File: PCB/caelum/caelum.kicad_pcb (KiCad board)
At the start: 2 copper layers, 14 parts, among them J1 BATT+, J2 BATT-, J3 3V3, J4 OUT-, Q1 FS8205A, U1 DW01A, U2 MCP1700T-3302E

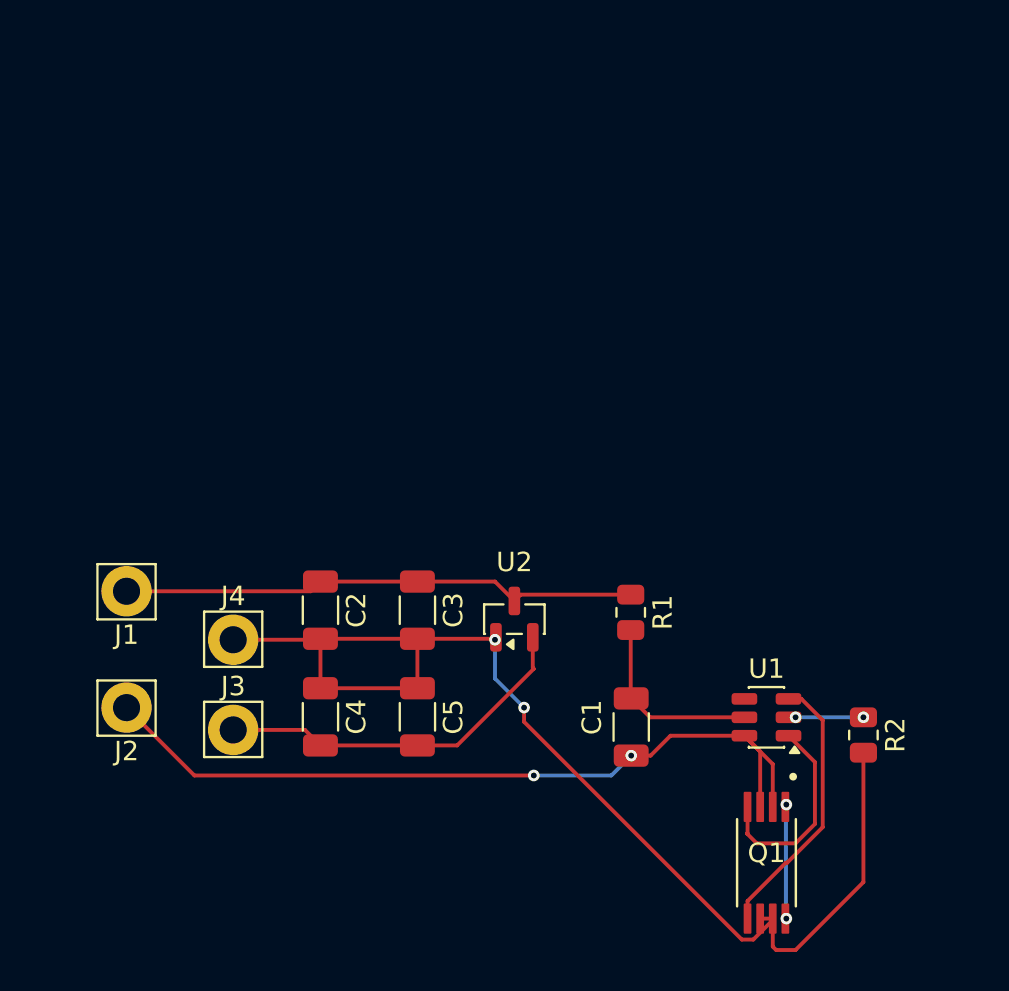
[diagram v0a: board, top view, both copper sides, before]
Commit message: Update partitions.csv for ESP32-H2 with 4MB Flash configuration
- Adjusted partition sizes and offsets to optimize for OTA updates.
- Reduced NVS size to 0x4000 and updated offsets for phy_init and otadata.
- Modified OTA partition sizes to fit within the new 4MB flash limit.
- Ensured compatibility with the new memory layout for better performance.
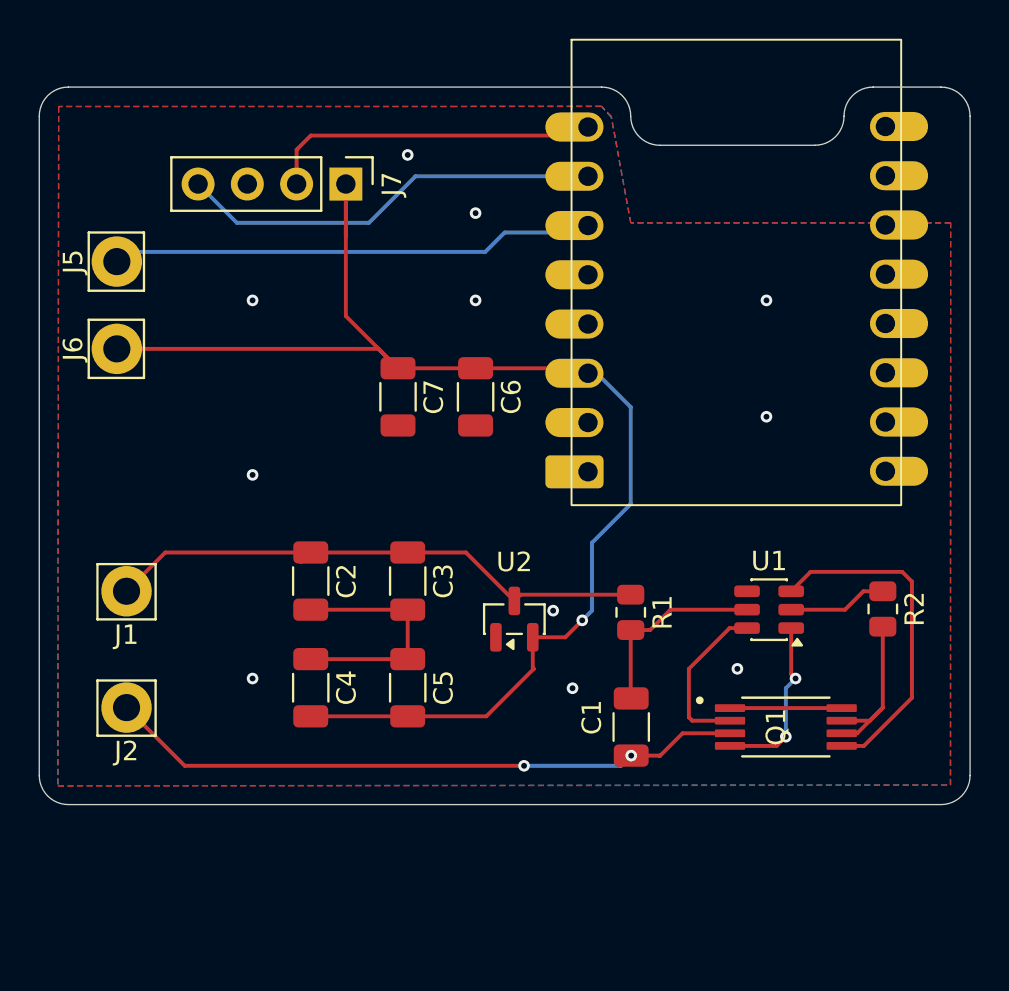
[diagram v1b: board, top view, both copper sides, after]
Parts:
- removed J3: 3V3, Connector_Pin:Pin_D1.4mm_L8.5mm_W2.8mm_FlatFork
- removed J4: OUT-, Connector_Pin:Pin_D1.4mm_L8.5mm_W2.8mm_FlatFork
- added C6: 1µF, Capacitor_SMD:C_1206_3216Metric, F.Cu at (80.0, 44.0)
- added C7: 0.1µF, Capacitor_SMD:C_1206_3216Metric, F.Cu at (76.0, 44.0)
- added J5: PulseIN, Connector_Pin:Pin_D1.4mm_L8.5mm_W2.8mm_FlatFork, F.Cu at (61.5, 37.0)
- added J6: PulseOUT, Connector_Pin:Pin_D1.4mm_L8.5mm_W2.8mm_FlatFork, F.Cu at (61.5, 41.5)
- added J7: Conn_01x04_Pin, Connector_PinHeader_2.54mm:PinHeader_1x04_P2.54mm_Vertical, F.Cu at (73.3, 33.0)
- added U3: ESP32-H2-SUPERMINI, esp32-h2-supermini:ESP32H2-Supermini, F.Cu at (92.9, 50.6)
- moved Q1 7.07 mm to (96.0, 61.0), turned to 0 degrees
- moved R2 6.58 mm to (101.0, 54.9)
- moved U1 5.55 mm to (95.1, 55.0)
- moved C2 1.58 mm to (71.5, 53.5)
- moved C3 1.58 mm to (76.5, 53.5)
- moved C4 1.58 mm to (71.5, 59.0)
- moved C5 1.58 mm to (76.5, 59.0)
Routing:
- net +3V3: track 19.1 -> 70.2 mm, vias 0 -> 1
- net OUT-: track 61.6 -> 21.8 mm, vias 2 -> 11
- net GPIO12: track 0.00 -> 25.1 mm
- net SCL: track 0.00 -> 21.9 mm
- net SDA: track 0.00 -> 17.3 mm
- net Net-(U1-OC): track 14.1 -> 17.5 mm
- net BATT+: track 26.8 -> 28.7 mm
- net Net-(U1-OD): track 10.6 -> 8.98 mm, vias 0 -> 2
- net Net-(U1-CS): track 3.86 -> 5.12 mm, vias 2 -> 0
- net BATT-: track 42.4 -> 41.6 mm
- net Net-(Q1-Pad1): track 6.04 -> 5.76 mm, vias 2 -> 0
- added copper zone on B.Cu, net OUT-
- added copper zone on F.Cu, net OUT-
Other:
- board outline added: 48 x 37 mm
